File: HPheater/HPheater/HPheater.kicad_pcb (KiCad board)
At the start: 2 copper layers, 100 x 100 mm, 6 parts, among them J1 Conn_01x02_Male

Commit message: started revision
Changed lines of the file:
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@@
       (outputformat 1)
       (mirror false)
-      (drillshape 1)
+      (drillshape 0)
       (scaleselection 1)
-      (outputdirectory "")
+      (outputdirectory "gerber/")
     )
   )
@@
     (fp_line (start 1.6 0.8) (end -1.6 0.8) (layer "F.Fab") (width 0.1))
     (fp_line (start -1.6 -0.8) (end 1.6 -0.8) (layer "F.Fab") (width 0.1))
-    (pad "1" smd roundrect (at -1.55 0 90) (size 1.3 1.75) (layers "F.Cu" "F.Paste" "F.Mask") (roundrect_rratio 0.192308)
+    (pad "1" smd roundrect (at -1.55 0 90) (size 1.3 1.75) (layers "F.Cu" "F.Paste" "F.Mask") (roundrect_rratio 0.1923076923)
       (net 1 "Net-(J1-Pad1)") (pintype "passive"))
-    (pad "2" smd roundrect (at 1.55 0 90) (size 1.3 1.75) (layers "F.Cu" "F.Paste" "F.Mask") (roundrect_rratio 0.192308)
+    (pad "2" smd roundrect (at 1.55 0 90) (size 1.3 1.75) (layers "F.Cu" "F.Paste" "F.Mask") (roundrect_rratio 0.1923076923)
       (net 2 "Net-(J1-Pad2)") (pintype "passive"))
     (model "${KICAD6_3DMODEL_DIR}/Resistor_SMD.3dshapes/R_1206_3216Metric.wrl"

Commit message: finished routing heater
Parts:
- removed R1: R, Resistor_SMD:R_1206_3216Metric_Pad1.30x1.75mm_HandSolder
- H1, H2, H3, H4: footprint MountingHole:MountingHole_2.2mm_M2_ISO14580 -> MountingHole:MountingHole_2.5mm
- J1: footprint connector_custom:AMASS_XT60PW-F -> HPfootprint:HEATER_CONTACT
- moved H2 120.6 mm to (171.0, 21.0)
- moved H3 96.6 mm to (171.0, 117.0)
- moved J1 90.0 mm to (185.5, 21.5)
- moved H4 88.5 mm to (267.0, 117.0)
- moved H1 8.50 mm to (267.0, 21.0)
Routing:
- net Net-(J1-Pin_1): track 6343.8 -> 6686.1 mm
- net Net-(J1-Pin_2): track 0.00 -> 198.3 mm
- removed copper zone on F.Cu, net Net-(J1-Pin_1)
- removed copper zone on F.Cu, net Net-(J1-Pin_2)
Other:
- outline, holes or cut-outs redrawn

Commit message: v3 routing
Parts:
- moved H1 62.3 mm to (220.0, 61.8)
- moved H2 62.3 mm to (124.0, 61.8)
- moved H4 62.3 mm to (220.0, 157.8)
- moved H3 62.3 mm to (124.0, 157.8)
- moved J1 52.1 mm to (136.2, 38.6)
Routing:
- net (no net): track 0.00 -> 9941.6 mm
- net Net-(J1-Pin_1): track 6686.1 -> 0.00 mm
- net Net-(J1-Pin_2): track 198.3 -> 0.00 mm
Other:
- board size 100 x 100 mm -> 100 x 120 mm

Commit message: routing
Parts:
- moved J1 35.9 mm to (172.0, 42.0)
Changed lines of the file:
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@@
 	(footprint "HPfootprint:HEATER_CONTACT"
 		(layer "F.Cu")
-		(at 136.2385 38.567999)
+		(at 172 42)
 		(property "Reference" "J1"
 			(at -2.1 -3 0)
@@
 			)
 		)
-		(property "Datasheet" ""
-			(at 0 0 0)
-			(layer "F.Fab")
-			(hide yes)
-			(effects
-				(font
-					(size 1.27 1.27)
-					(thickness 0.15)
-				)
-			)
-		)
-		(property "Description" "Generic connector, single row, 01x02, script generated (kicad-library-utils/schlib/autogen/connector/)"
-			(at 0 0 0)
-			(layer "F.Fab")
-			(hide yes)
-			(effects
-				(font
-					(size 1.27 1.27)
-					(thickness 0.15)
-				)
-			)
-		)
+		(property "Datasheet" "~"
+			(at 0 0 0)
+			(layer "F.Fab")
+			(hide yes)
+			(effects
+				(font
+					(size 1.27 1.27)
+					(thickness 0.15)
+				)
+			)
+		)
+		(property "Description" ""
+			(at 0 0 0)
+			(layer "F.Fab")
+			(hide yes)
+			(effects
+				(font
+					(size 1.27 1.27)
+					(thickness 0.15)
+				)
+			)
+		)
+		(property ki_fp_filters "Connector*:*_1x??_*")
+		(sheetname "/")
 		(sheetfile "HPheater.kicad_sch")
 		(attr smd)
@@
 		)
 		(pad "1" smd roundrect
-			(at -2.75 0)
-			(size 3 4.5)
+			(at -9.25 0 90)
+			(size 3 15)
 			(layers "F.Cu" "F.Mask" "F.Paste")
 			(roundrect_rratio 0.25)
@@
 		)
 		(pad "2" smd roundrect
-			(at 2.75 0)
-			(size 3 4.5)
+			(at 9.25 0 90)
+			(size 3 15)
 			(layers "F.Cu" "F.Mask" "F.Paste")
 			(roundrect_rratio 0.25)
@@
 			)
 		)
-		(property "Datasheet" ""
-			(at 0 0 0)
-			(layer "F.Fab")
-			(hide yes)
-			(effects
-				(font
-					(size 1.27 1.27)
-					(thickness 0.15)
-				)
-			)
-		)
-		(property "Description" "Mounting Hole without connection"
-			(at 0 0 0)
-			(layer "F.Fab")
-			(hide yes)
-			(effects
-				(font
-					(size 1.27 1.27)
-					(thickness 0.15)
-				)
-			)
-		)
+		(property "Datasheet" "~"
+			(at 0 0 0)
+			(layer "F.Fab")
+			(hide yes)
+			(effects
+				(font
+					(size 1.27 1.27)
+					(thickness 0.15)
+				)
+			)
+		)
+		(property "Description" ""
+			(at 0 0 0)
+			(layer "F.Fab")
+			(hide yes)
+			(effects
+				(font
+					(size 1.27 1.27)
+					(thickness 0.15)
+				)
+			)
+		)
+		(property ki_fp_filters "MountingHole*")
+		(sheetname "/")
 		(sheetfile "HPheater.kicad_sch")
 		(attr exclude_from_pos_files)
@@
 			)
 		)
-		(property "Datasheet" ""
-			(at 0 0 0)
-			(layer "F.Fab")
-			(hide yes)
-			(effects
-				(font
-					(size 1.27 1.27)
-					(thickness 0.15)
-				)
-			)
-		)
-		(property "Description" "Mounting Hole without connection"
-			(at 0 0 0)
-			(layer "F.Fab")
-			(hide yes)
-			(effects
-				(font
-					(size 1.27 1.27)
-					(thickness 0.15)
-				)
-			)
-		)
+		(property "Datasheet" "~"
+			(at 0 0 0)
+			(layer "F.Fab")
+			(hide yes)
+			(effects
+				(font
+					(size 1.27 1.27)
+					(thickness 0.15)
+				)
+			)
+		)
+		(property "Description" ""
+			(at 0 0 0)
+			(layer "F.Fab")
+			(hide yes)
+			(effects
+				(font
+					(size 1.27 1.27)
+					(thickness 0.15)
+				)
+			)
+		)
+		(property ki_fp_filters "MountingHole*")
+		(sheetname "/")
 		(sheetfile "HPheater.kicad_sch")
 		(attr exclude_from_pos_files)
@@
 			)
 		)
-		(property "Datasheet" ""
-			(at 0 0 0)
-			(layer "F.Fab")
-			(hide yes)
-			(effects
-				(font
-					(size 1.27 1.27)
-					(thickness 0.15)
-				)
-			)
-		)
-		(property "Description" "Mounting Hole without connection"
-			(at 0 0 0)
-			(layer "F.Fab")
-			(hide yes)
-			(effects
-				(font
-					(size 1.27 1.27)
-					(thickness 0.15)
-				)
-			)
-		)
+		(property "Datasheet" "~"
+			(at 0 0 0)
+			(layer "F.Fab")
+			(hide yes)
+			(effects
+				(font
+					(size 1.27 1.27)
+					(thickness 0.15)
+				)
+			)
+		)
+		(property "Description" ""
+			(at 0 0 0)
+			(layer "F.Fab")
+			(hide yes)
+			(effects
+				(font
+					(size 1.27 1.27)
+					(thickness 0.15)
+				)
+			)
+		)
+		(property ki_fp_filters "MountingHole*")
+		(sheetname "/")
 		(sheetfile "HPheater.kicad_sch")
 		(attr exclude_from_pos_files)
@@
 			)
 		)
-		(property "Datasheet" ""
-			(at 0 0 0)
-			(layer "F.Fab")
-			(hide yes)
-			(effects
-				(font
-					(size 1.27 1.27)
-					(thickness 0.15)
-				)
-			)
-		)
-		(property "Description" "Mounting Hole without connection"
-			(at 0 0 0)
-			(layer "F.Fab")
-			(hide yes)
-			(effects
-				(font
-					(size 1.27 1.27)
-					(thickness 0.15)
-				)
-			)
-		)
+		(property "Datasheet" "~"
+			(at 0 0 0)
+			(layer "F.Fab")
+			(hide yes)
+			(effects
+				(font
+					(size 1.27 1.27)
+					(thickness 0.15)
+				)
+			)
+		)
+		(property "Description" ""
+			(at 0 0 0)
+			(layer "F.Fab")
+			(hide yes)
+			(effects
+				(font
+					(size 1.27 1.27)
+					(thickness 0.15)
+				)
+			)
+		)
+		(property ki_fp_filters "MountingHole*")
+		(sheetname "/")
 		(sheetfile "HPheater.kicad_sch")
 		(attr exclude_from_pos_files)

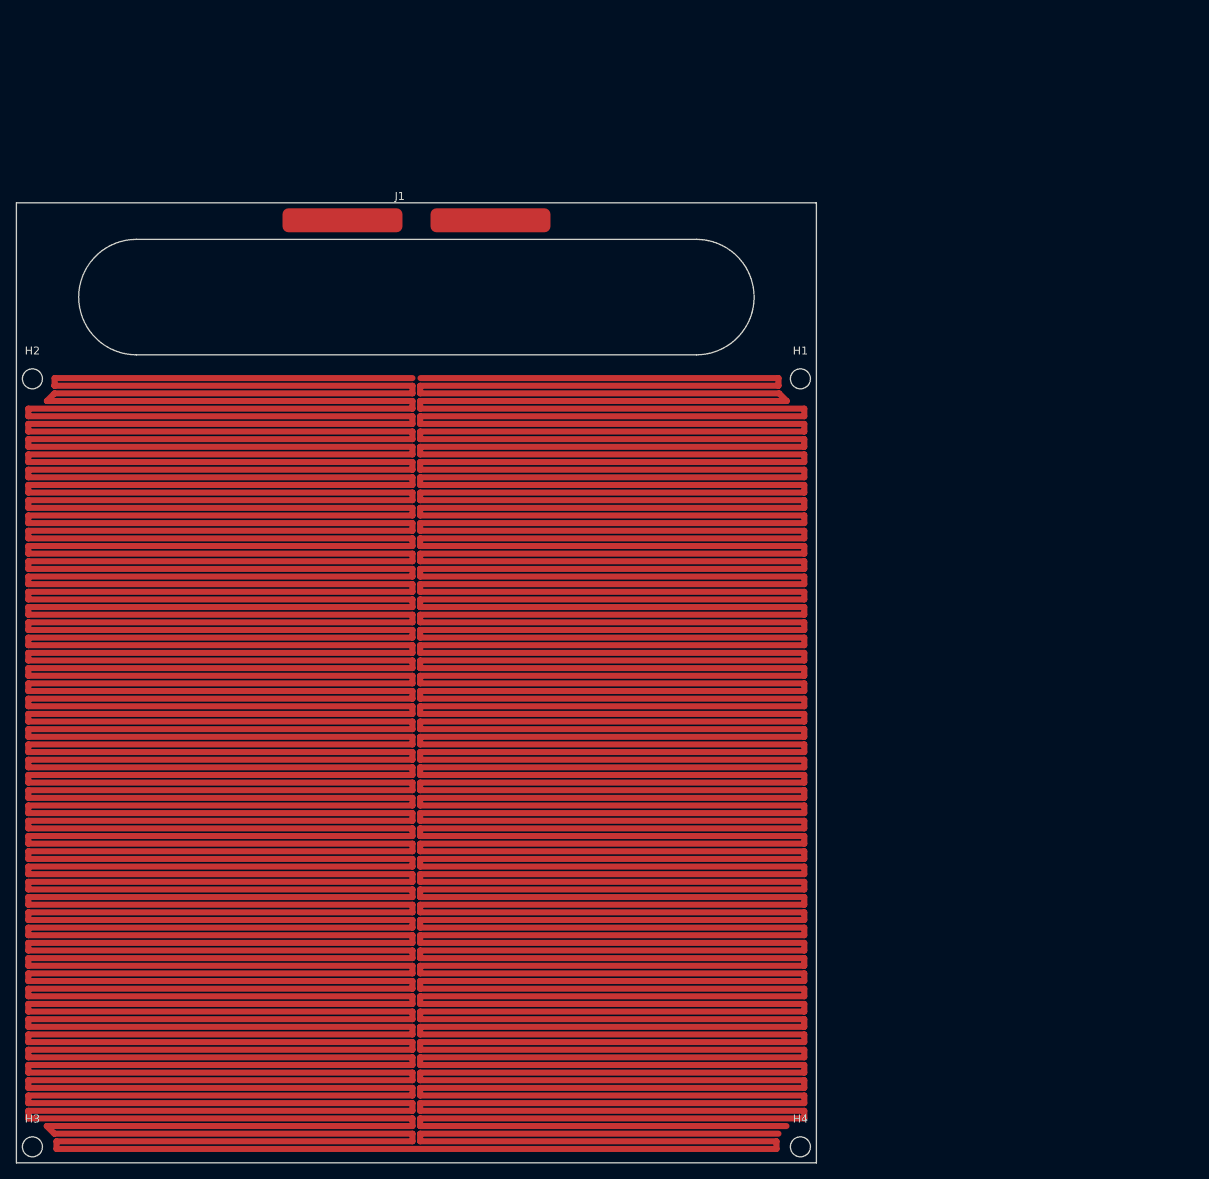
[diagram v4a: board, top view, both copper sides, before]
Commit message: fixed open on heater
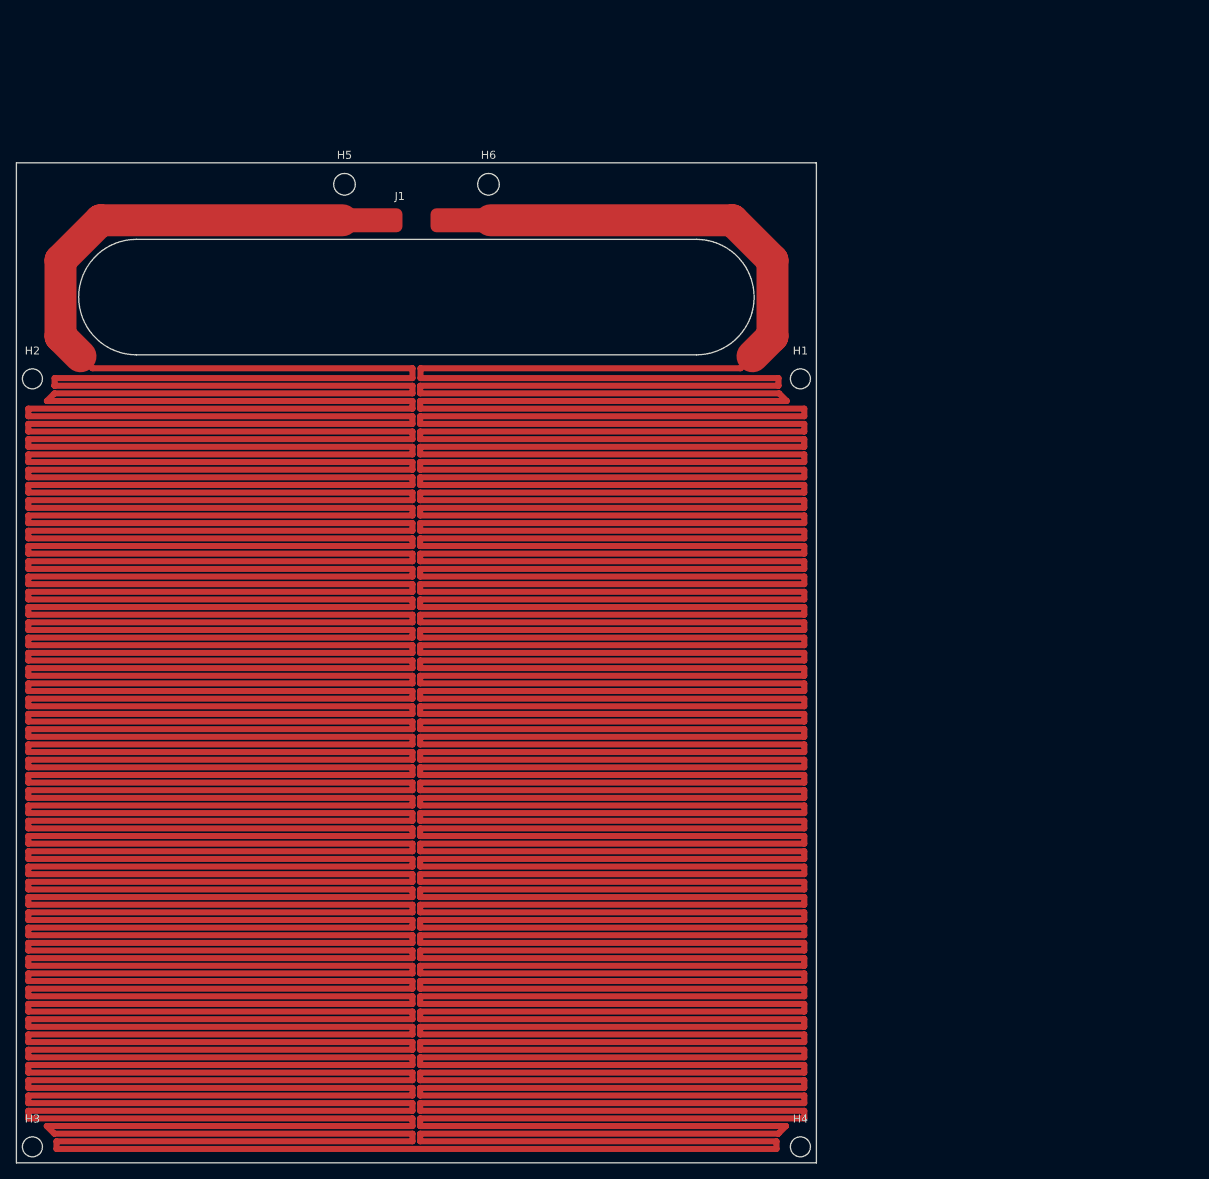
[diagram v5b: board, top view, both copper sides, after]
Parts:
- added H5: MountingHole, MountingHole:MountingHole_2.7mm_M2.5, F.Cu at (163.0, 37.5)
- added H6: MountingHole, MountingHole:MountingHole_2.7mm_M2.5, F.Cu at (181.0, 37.5)
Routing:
- net (no net): track 9941.6 -> 0.00 mm
- net Net-(J1-Pin_1): track 0.00 -> 5201.2 mm
- net Net-(J1-Pin_2): track 0.00 -> 4929.1 mm
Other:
- board size 100 x 120 mm -> 100 x 125 mm
